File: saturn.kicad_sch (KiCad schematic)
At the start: 101 parts, among them J1 Conn_01x04_Pin, J10 Conn_01x04, J11 USB_B_Micro, J12 USB_C_Receptacle_USB2.0, J13 ZX-XH2.54-3PWT, J14 Conn_01x04_Pin, J2 PMOD3_FULL, J3 Conn_01x06, J4 Conn_01x06, J6 ZX-XH2.54-10PWT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

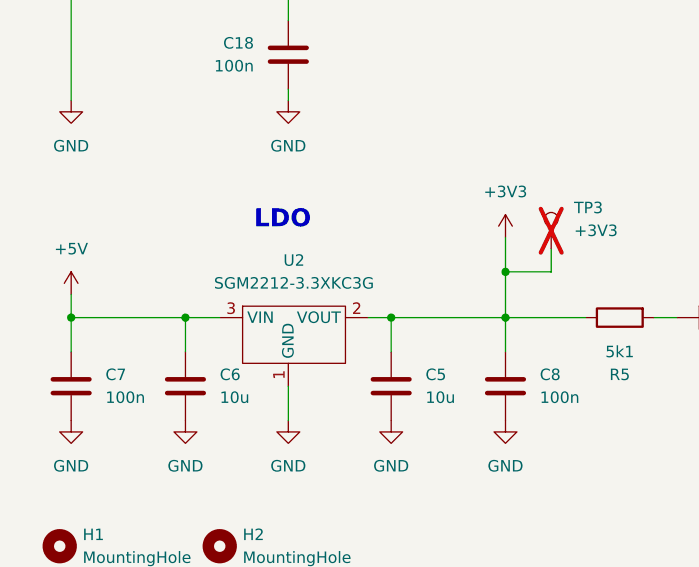
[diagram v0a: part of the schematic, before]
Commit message: Use AMS1117-3.3 LDO (cheaper)
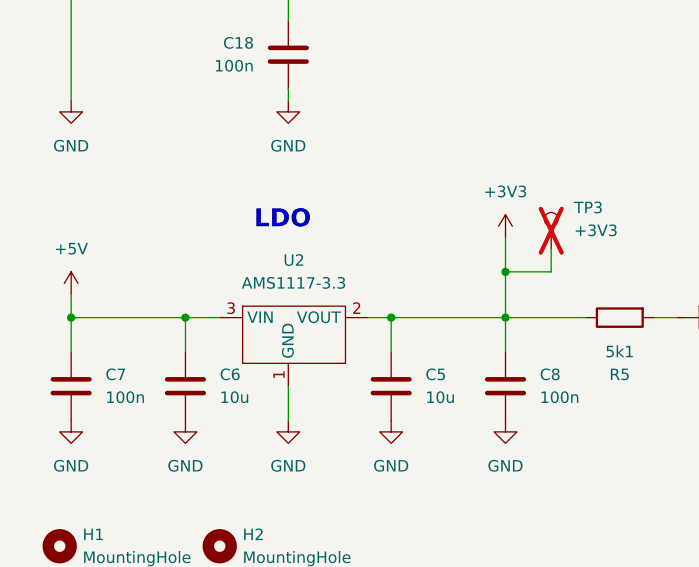
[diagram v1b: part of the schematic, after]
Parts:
- U2: value SGM2212-3.3XKC3G -> AMS1117-3.3; LCSC C3294699 -> C6186
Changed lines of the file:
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@@
 			)
 		)
-		(property "Value" "SGM2212-3.3XKC3G"
+		(property "Value" "AMS1117-3.3"
 			(at 46.355 241.3 0)
 			(show_name no)
@@
 			)
 		)
-		(property "LCSC" "C3294699"
+		(property "LCSC" "C6186"
 			(at 45.72 243.84 0)
 			(hide yes)

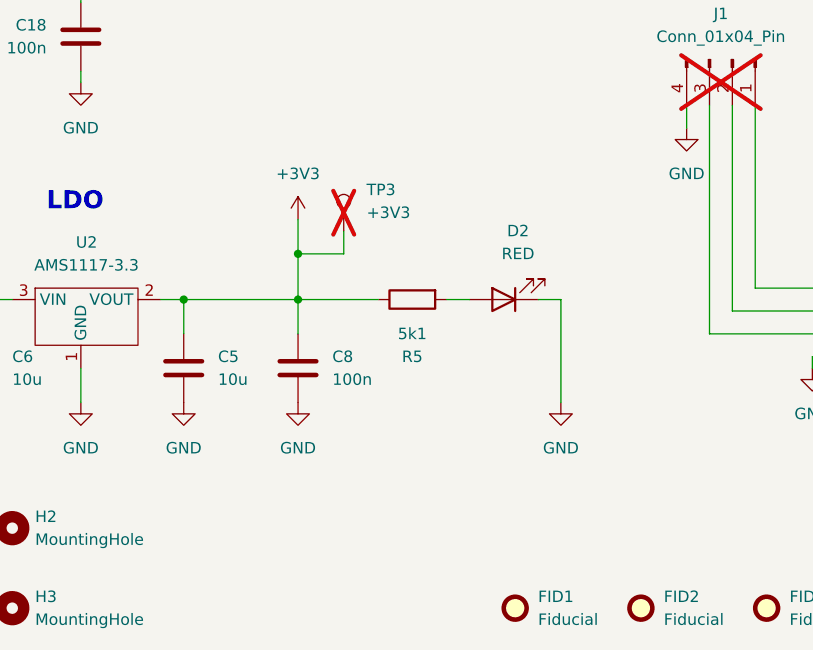
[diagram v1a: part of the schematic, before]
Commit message: Add LDO output cap series resistance
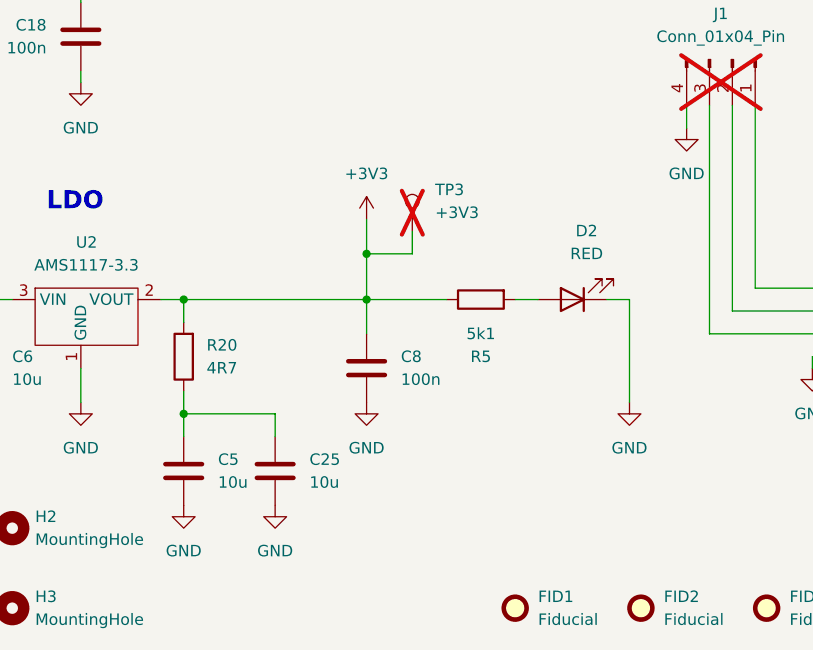
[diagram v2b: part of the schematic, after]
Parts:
- added C25: 10u, Capacitor_SMD:C_0805_2012Metric, symbol Device:C
- added R20: 4R7, Resistor_SMD:R_0805_2012Metric, symbol Device:R
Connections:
- net +3V3: now also R20.2; no longer C5.1
- net GND: now also C25.2
- new net: C25.1, C5.1, R20.1
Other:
- moved on the sheet: C5, C8, D2, R5, TP3

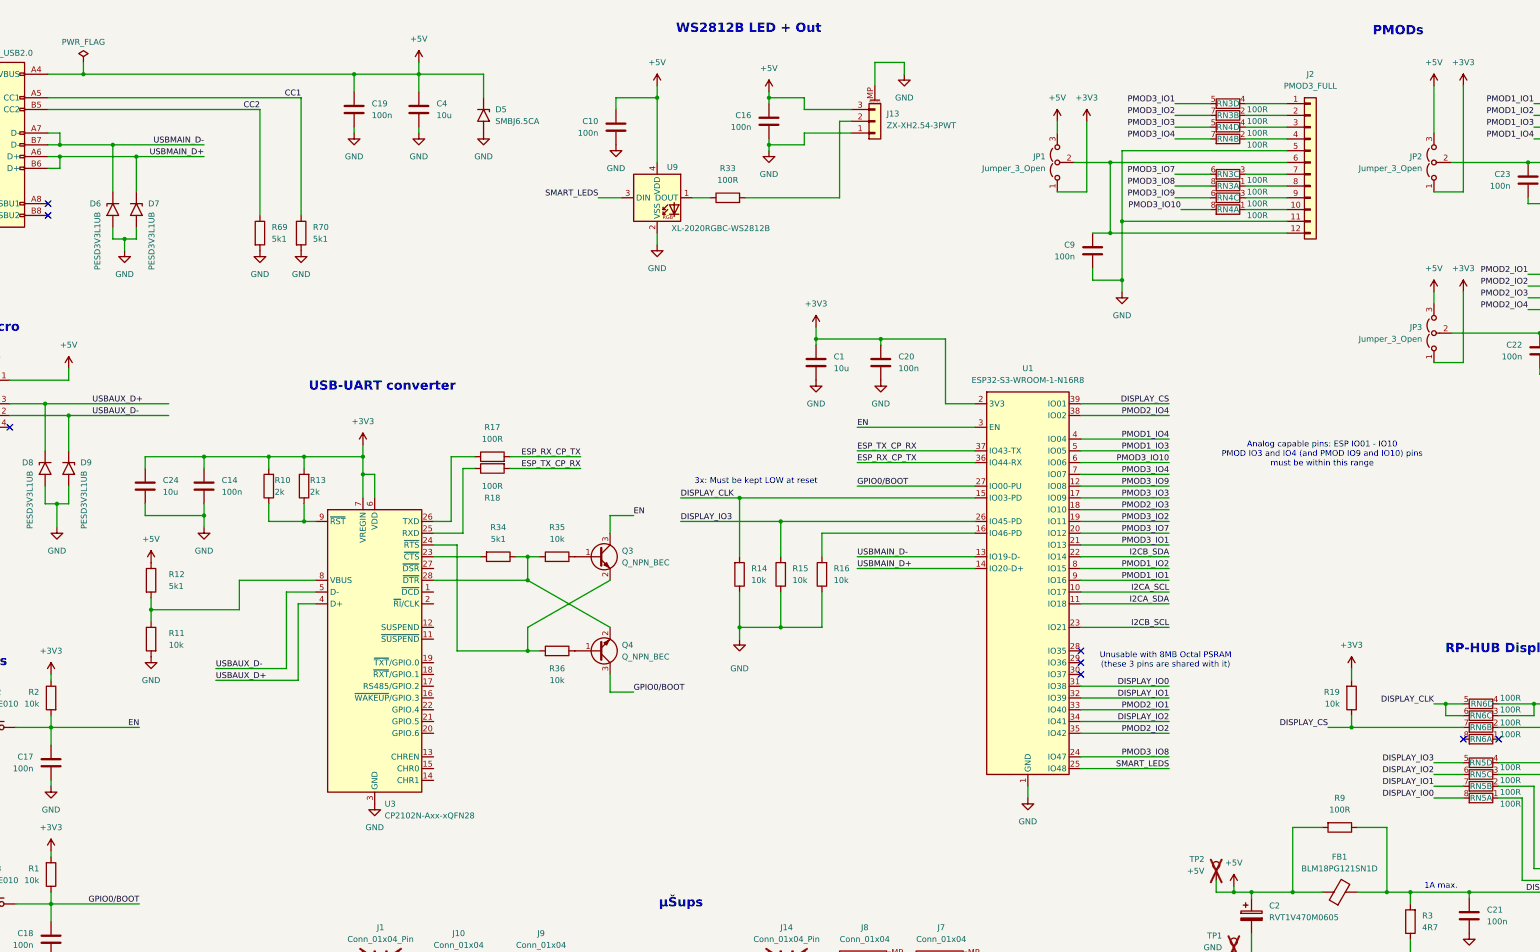
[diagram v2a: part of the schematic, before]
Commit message: Separate LED Strip to IO46 with level shift, tune layout
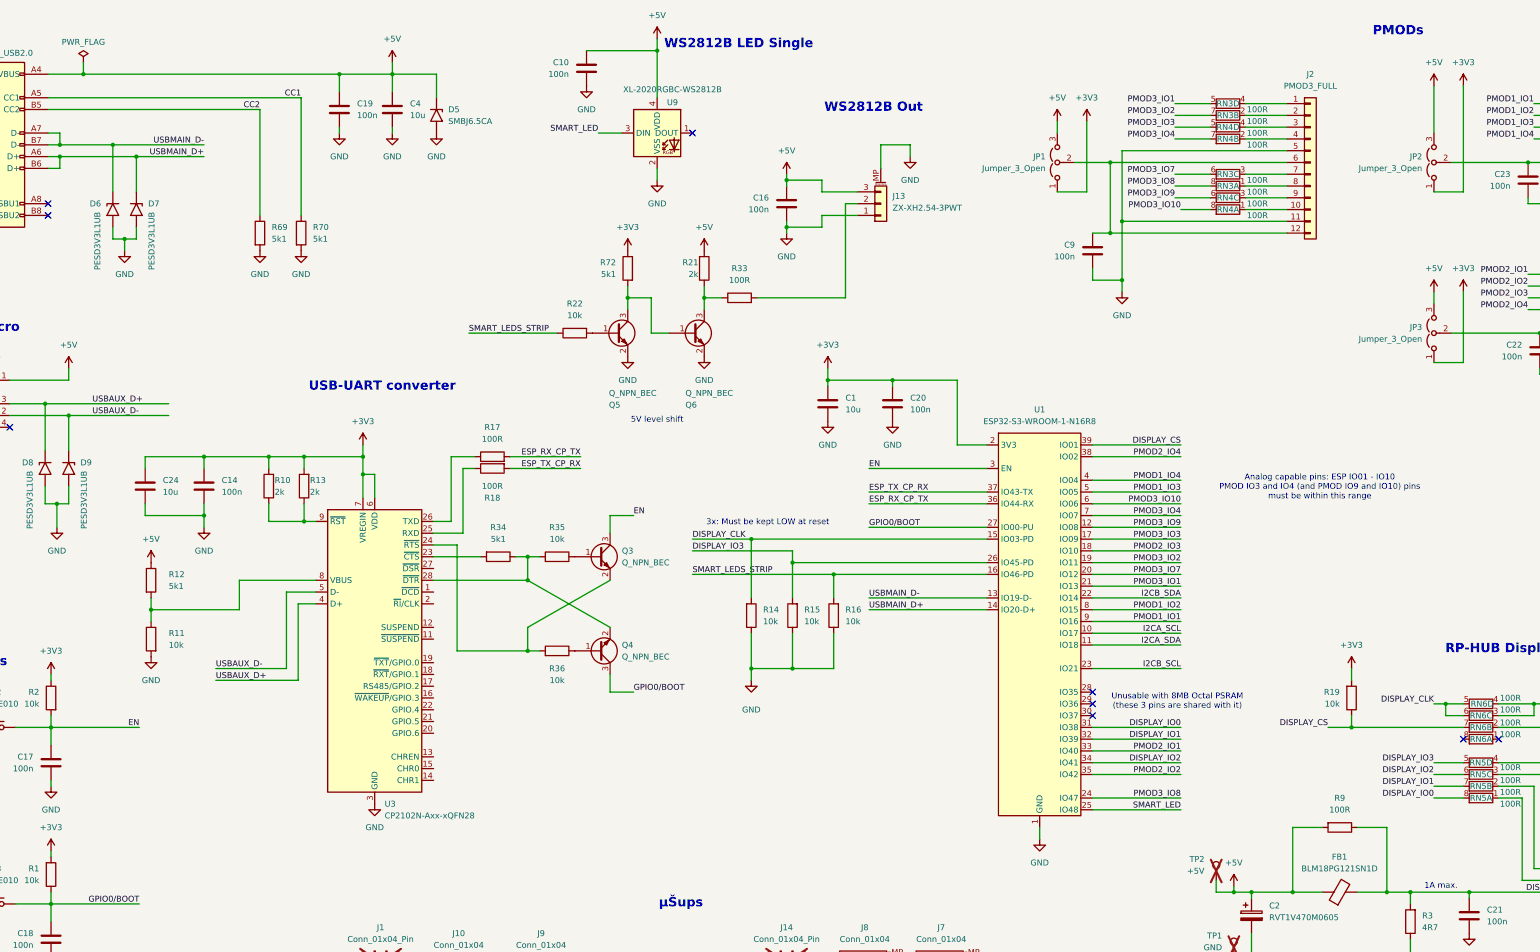
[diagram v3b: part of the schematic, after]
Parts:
- added Q5, Q6: Q_NPN_BEC, Package_TO_SOT_SMD:SOT-23, symbol Device:Q_NPN_BEC
- added R21: 2k, Resistor_SMD:R_0402_1005Metric, symbol Device:R
- added R22: 10k, Resistor_SMD:R_0402_1005Metric, symbol Device:R
- added R72: 5k1, Resistor_SMD:R_0402_1005Metric, symbol Device:R
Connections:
- net +3V3: now also R72.1
- net +5V: now also R21.2
- net GND: now also Q5.2 (E), Q6.2 (E)
- net at R33.1: now also Q6.3 (C), R21.1; no longer U9.1 (DOUT)
- net SMART_LEDS_STRIP: now reaches R16.2, U1.16 (IO46-PD)
- net SMART_LEDS_STRIP: now also R22.1
- net SMART_LEDS renamed SMART_LED
- new net: Q5.3 (C), Q6.1 (B), R72.2
- new net: Q5.1 (B), R22.2
- no-connect marks 8 -> 9
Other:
- note added: "5V level shift"
- note added: "WS2812B LED Single"
- note added: "WS2812B Out"
- note removed: "WS2812B LED + Out"
- moved on the sheet: C1, C10, C16, C19, C20, C4, D5, J13, R14, R15, R16, R33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

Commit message: Tune layout, POS corrections, kik.json
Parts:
- added T1, T2, T3, T4: Tab, kikit:Tab, symbol kikit:Tab
- J11: JLCPCB_CORRECTION (none) -> 0;-0.1;0
- J12: JLCPCB_CORRECTION 0;-1;0 -> 0;-1.2;0
- U1: JLCPCB_CORRECTION 0;9;0 -> 0;9.1;0

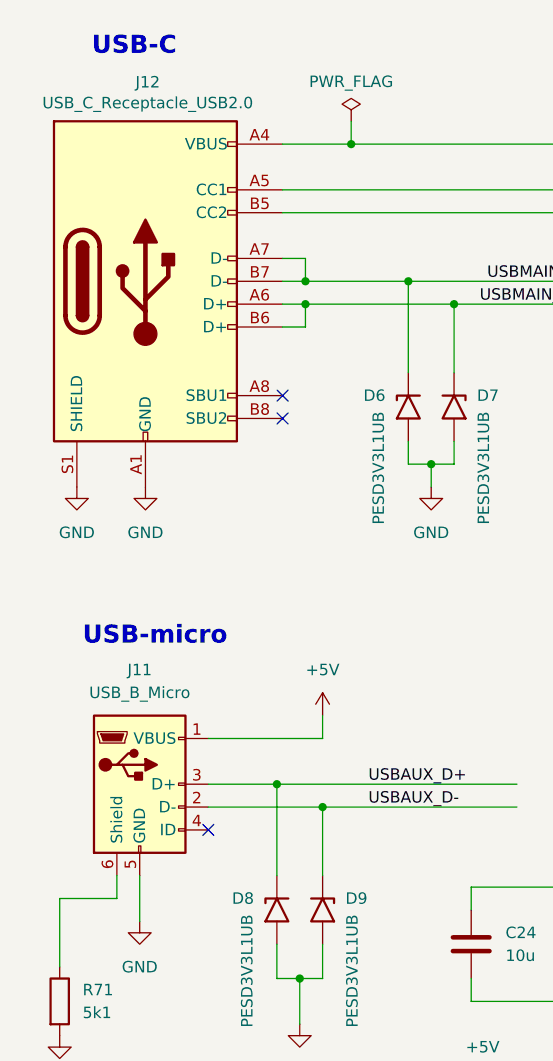
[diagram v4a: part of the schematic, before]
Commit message: Replace Micro-USB connector
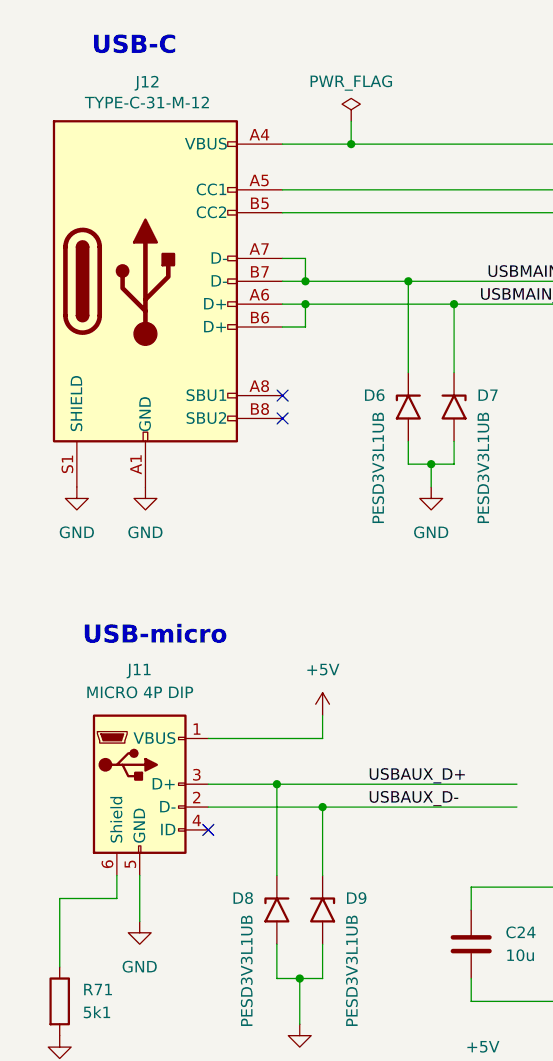
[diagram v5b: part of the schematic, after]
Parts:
- J11: value USB_B_Micro -> MICRO 4P DIP; footprint USB_Conn:USB_Micro-B_XNJ-073_With_THR_Paste -> USB_Conn:USB_MICRO 4P DIP; JLCPCB_CORRECTION 0;-0.1;0 -> 0;-0;0; LCSC C404969 -> C456008; Price (100ks) 0.0269 -> (none); Price (1ks) 0.0329 -> (none)
- J12: value USB_C_Receptacle_USB2.0 -> TYPE-C-31-M-12; JLCPCB_CORRECTION 0;-1.2;0 -> 0;-1.4;0
- U1: JLCPCB_CORRECTION 0;9.1;0 -> 0;8.9;0
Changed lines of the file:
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@@
 	(wire
 		(pts
-			(xy 26.67 113.03) (xy 26.67 110.49)
-		)
-		(stroke
-			(width 0)
-			(type default)
-		)
-	)
-	(wire
-		(pts
 			(xy 44.45 118.11) (xy 44.45 121.92)
 		)
@@
 	(wire
 		(pts
+			(xy 26.67 110.49) (xy 26.67 113.03)
+		)
+		(stroke
+			(width 0)
+			(type default)
+		)
+	)
+	(wire
+		(pts
 			(xy 148.59 148.59) (xy 148.59 153.67)
 		)
@@
 			)
 		)
-		(property "Value" "USB_B_Micro"
+		(property "Value" "MICRO 4P DIP"
 			(at 29.21 90.17 0)
 			(show_name no)
@@
 			)
 		)
-		(property "Footprint" "USB_Conn:USB_Micro-B_XNJ-073_With_THR_Paste"
+		(property "Footprint" "USB_Conn:USB_MICRO 4P DIP"
 			(at 33.02 101.6 0)
 			(hide yes)
@@
 			)
 		)
-		(property "LCSC" "C404969"
+		(property "LCSC" "C456008"
 			(at 29.21 100.33 0)
 			(hide yes)
@@
 			)
 		)
-		(property "JLCPCB_CORRECTION" "0;-0.1;0"
+		(property "JLCPCB_CORRECTION" "0;-0;0"
 			(at 29.21 100.33 0)
 			(hide yes)
@@
 			)
 		)
-		(property "Price (100ks)" "0.0269"
-			(at 29.21 100.33 0)
-			(hide yes)
-			(show_name no)
-			(do_not_autoplace no)
-			(effects
-				(font
-					(size 1.27 1.27)
-				)
-			)
-		)
-		(property "Price (1ks)" "0.0329"
-			(at 29.21 100.33 0)
-			(hide yes)
-			(show_name no)
-			(do_not_autoplace no)
-			(effects
-				(font
-					(size 1.27 1.27)
-				)
-			)
-		)
 		(pin "1"
 		)
@@
 			)
 		)
-		(property "JLCPCB_CORRECTION" "0;9.1;0"
+		(property "JLCPCB_CORRECTION" "0;8.9;0"
 			(at 259.08 106.68 0)
 			(hide yes)
@@
 			)
 		)
-		(property "Value" "USB_C_Receptacle_USB2.0"
+		(property "Value" "TYPE-C-31-M-12"
 			(at 30.099 24.638 0)
 			(show_name no)
@@
 			)
 		)
-		(property "JLCPCB_CORRECTION" "0;-1.2;0"
+		(property "JLCPCB_CORRECTION" "0;-1.4;0"
 			(at 29.845 44.45 0)
 			(hide yes)
